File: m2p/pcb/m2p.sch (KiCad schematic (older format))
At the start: 78 parts, among them IC1 APU1205-HF-3, IC2 ADuM1201, IC3 SP100-2T, IC4 ADXL375, IC5 STM32F103C, P1 CONN_2, P2 CONN_4, P3 CONN_2, P4 SWD, P5 CONN_2, P6 CONN_2, Q1 MOSFET_P, Q2 MOSFET_P, Q3 MOSFET_N, Q4 MOSFET_N, U1 BAT BOX, U2 ARM SW, U3 RG LED, X1 8M

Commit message: add first go at m2r schematic
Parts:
- IC1: Farnell (none) -> 2319654
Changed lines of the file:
@@
 F 2 "" H 1650 850 60  0001 C CNN
 F 3 "" H 1650 850 60  0001 C CNN
+F 4 "2319654" H 1650 850 60  0001 C CNN "Farnell"
 	1    1650 850
 	1    0    0    -1

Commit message: finish up m2r schematic
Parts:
- added TP1, TP10, TP11, TP12, TP13, TP14, TP15, TP16, TP17, TP18, TP19, TP2, TP20, TP21, TP22, TP3, TP4, TP5, TP6, TP7, TP8, TP9: TESTPAD, symbol TESTPAD
- P3: Farnell (none) -> 1462926
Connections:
- net +BATT: now also TP1.1 (TP)
- net ACCEL_CS: now also TP9.1 (TP)
- net ACCEL_INT1: now also TP7.1 (TP)
- net ACCEL_INT2: now also TP8.1 (TP)
- net ACCEL_MISO: now also TP11.1 (TP)
- net ACCEL_MOSI: now also TP12.1 (TP)
- net ACCEL_SCK: now also TP10.1 (TP)
- net BARO_CS: now also TP19.1 (TP)
- net BARO_MISO: now also TP21.1 (TP)
- net BARO_MOSI: now also TP22.1 (TP)
- net BARO_SCK: now also TP20.1 (TP)
- net BAT_MON: now also TP6.1 (TP)
- net GND: now also TP3.1 (TP)
- net PYRO_1_C: now also TP16.1 (TP)
- net PYRO_1_F: now also TP15.1 (TP)
- net PYRO_2_C: now also TP18.1 (TP)
- net PYRO_2_F: now also TP17.1 (TP)
- net SER_IN: now also TP14.1 (TP)
- net SER_OUT: now also TP13.1 (TP)
- net VCC: now also TP2.1 (TP)
- net at IC2.7 (IN_A), P2.2 (P2): now also TP4.1 (TP)
- net at IC2.6 (OUT_B), P2.3 (P3): now also TP5.1 (TP)

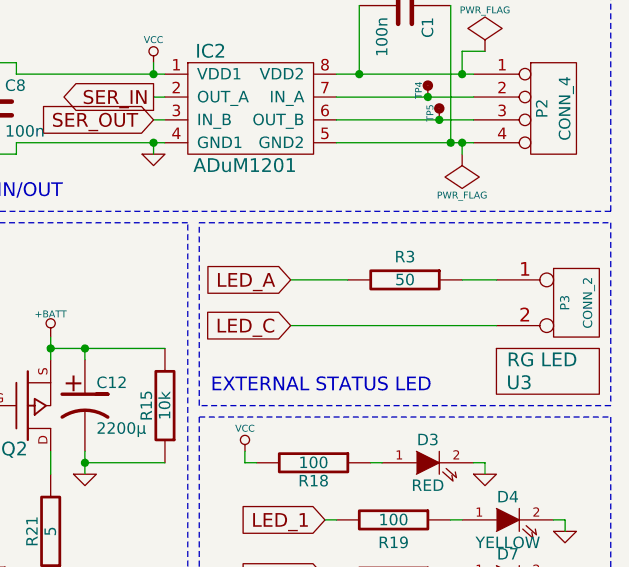
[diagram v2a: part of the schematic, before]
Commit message: swap 50R to two 100R on m2p too
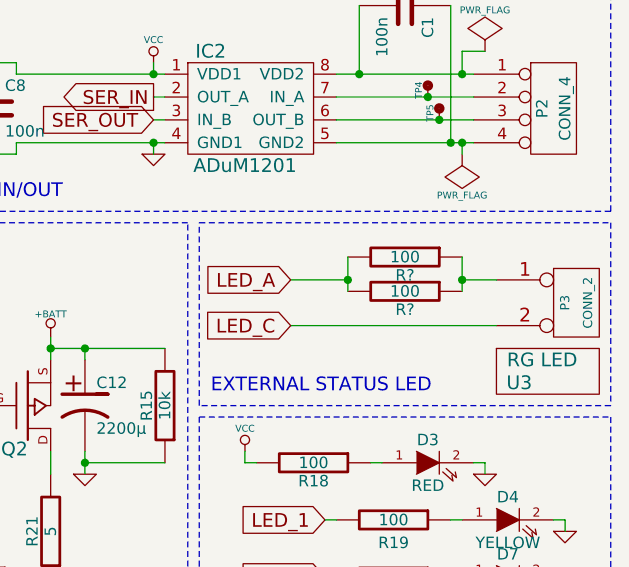
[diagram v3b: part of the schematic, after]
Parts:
- removed R3: 50, 0603, symbol R
- added R? (x2): 100, 0603, symbol R
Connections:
- net LED_A: now also R?.2, R?.2
- net at P3.1 (P1): now also R?.1, R?.1
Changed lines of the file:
@@
-	0    1    1    0
-$EndComp
-$Comp
-L R R3
-U 1 1 53683E31
-P 10250 1850
-F 0 "R3" V 10150 1850 50  0000 C CNN
-F 1 "50" V 10250 1850 50  0000 C CNN
-F 2 "0603" H 10250 1850 60  0001 C CNN
-F 3 "" H 10250 1850 60  0001 C CNN
-F 4 "2331983" V 10250 1850 60  0001 C CNN "Farnell"
-	1    10250 1850
 	0    1    1    0
 $EndComp
@@
 Connection ~ 10350 1050
 Connection ~ 10400 1150
+$Comp
+L R R?
+U 1 1 537E9CA5
+P 10250 1900
+F 0 "R?" V 10330 1900 50  0000 C CNN
+F 1 "100" V 10250 1900 50  0000 C CNN
+F 2 "0603" H 10250 1900 60  0001 C CNN
+F 3 "" H 10250 1900 60  0001 C CNN
+F 4 "2331989" V 10250 1900 60  0001 C CNN "Farnell"
+	1    10250 1900
+	0    1    1    0
+$EndComp
+$Comp
+L R R?
+U 1 1 537E9E87
+P 10250 1750
+F 0 "R?" V 10330 1750 50  0000 C CNN
+F 1 "100" V 10250 1750 50  0000 C CNN
+F 2 "0603" H 10250 1750 60  0001 C CNN
+F 3 "" H 10250 1750 60  0001 C CNN
+F 4 "2331989" V 10250 1750 60  0001 C CNN "Farnell"
+	1    10250 1750
+	0    1    1    0
+$EndComp
+Wire Wire Line
+	10000 1750 10000 1900
+Connection ~ 10000 1850
+Wire Wire Line
+	10500 1750 10500 1900
+Connection ~ 10500 1850
 $EndSCHEMATC

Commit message: oops, annotate
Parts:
- gave numbers to parts that had none: 2
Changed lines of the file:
@@
 Connection ~ 10400 1150
 $Comp
-L R R?
+L R R29
 U 1 1 537E9CA5
 P 10250 1900
-F 0 "R?" V 10330 1900 50  0000 C CNN
+F 0 "R29" V 10330 1900 50  0000 C CNN
 F 1 "100" V 10250 1900 50  0000 C CNN
 F 2 "0603" H 10250 1900 60  0001 C CNN
@@
 $EndComp
 $Comp
-L R R?
+L R R3
 U 1 1 537E9E87
 P 10250 1750
-F 0 "R?" V 10330 1750 50  0000 C CNN
+F 0 "R3" V 10330 1750 50  0000 C CNN
 F 1 "100" V 10250 1750 50  0000 C CNN
 F 2 "0603" H 10250 1750 60  0001 C CNN

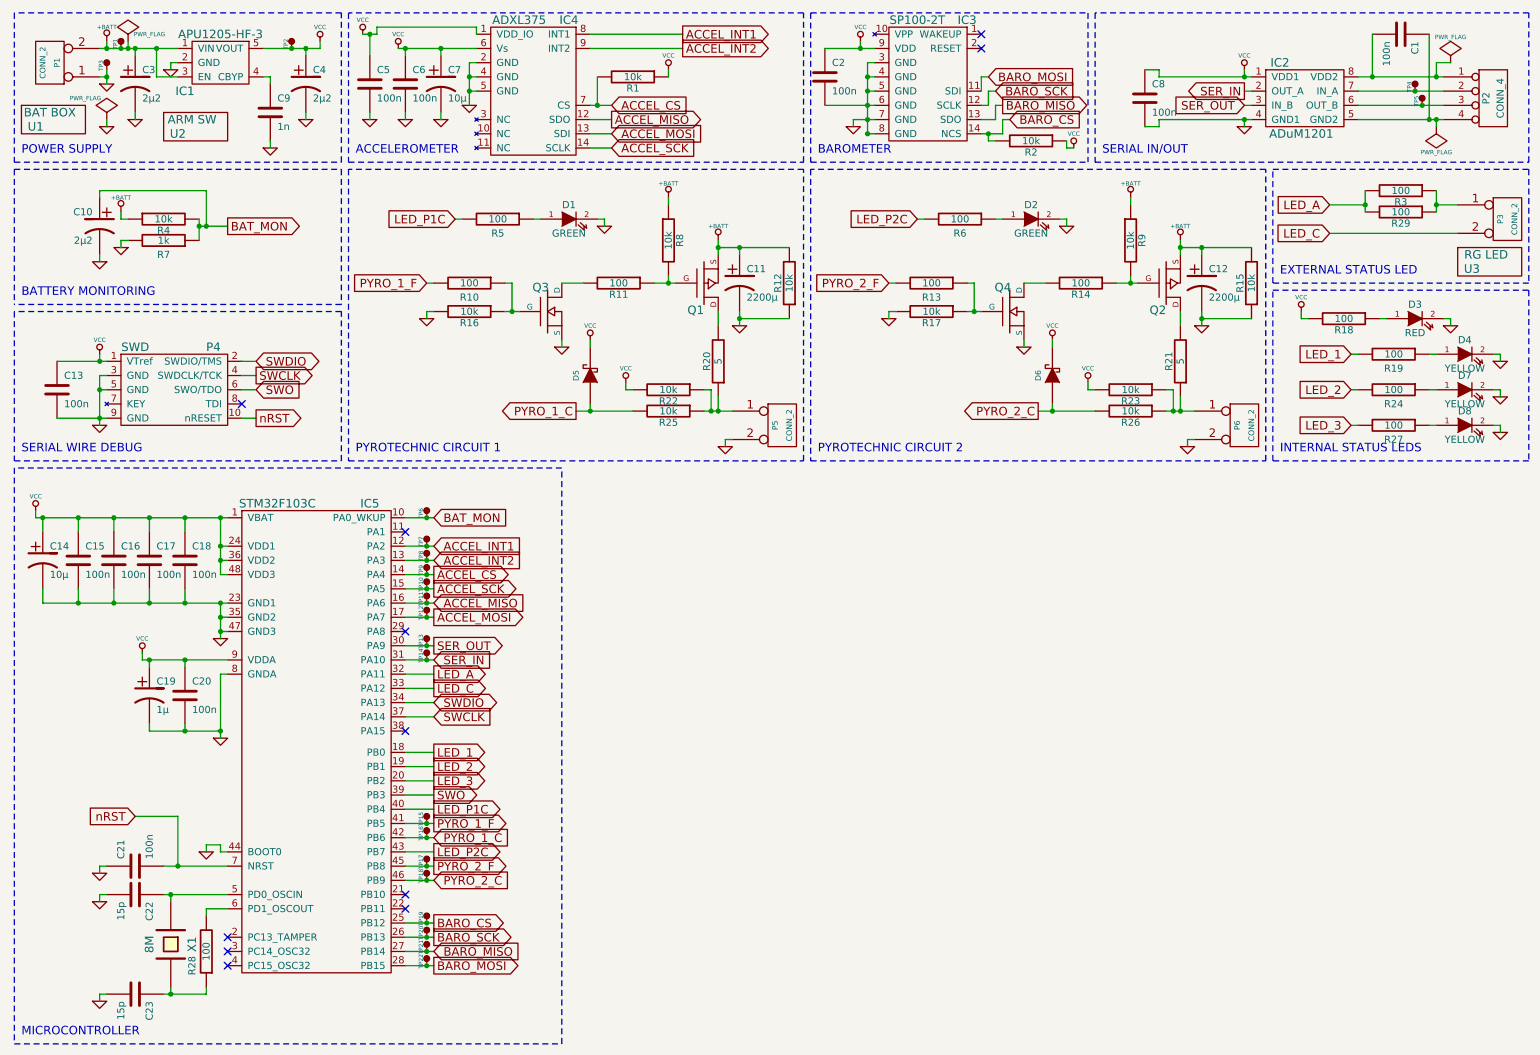
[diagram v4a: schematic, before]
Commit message: add separate connector for arming switch to m2p
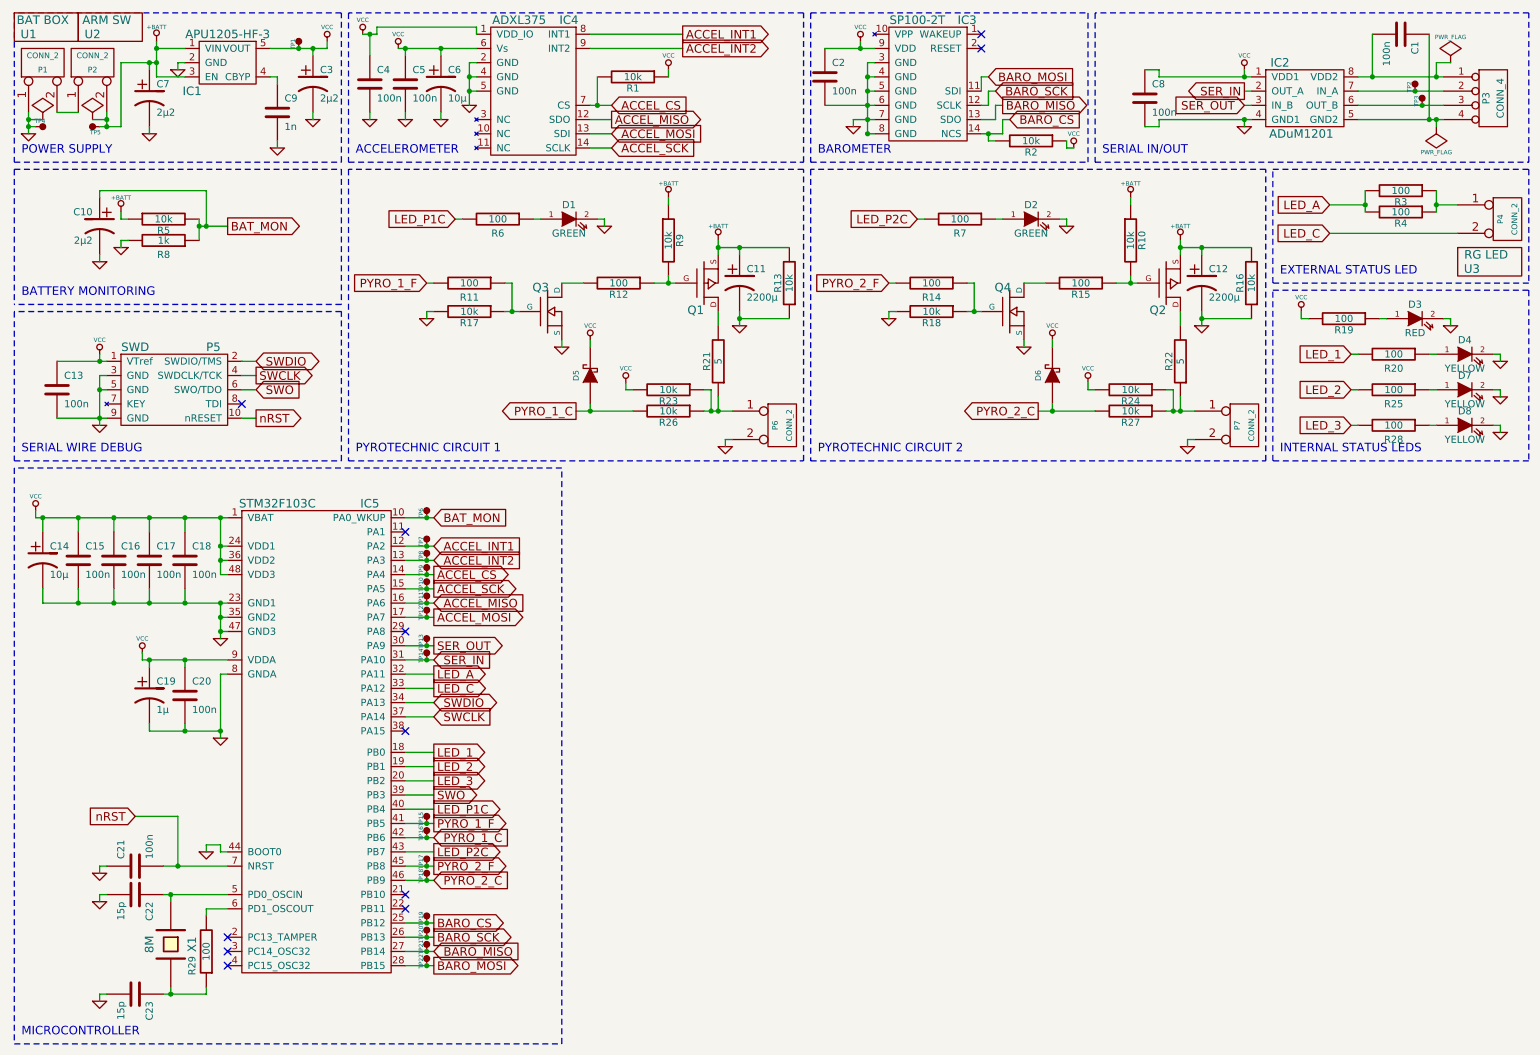
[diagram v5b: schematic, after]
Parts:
- added P2: CONN_2, symbol CONN_2
- renumbered C4 to C3, C5 to C4, C6 to C5, C7 to C6, C3 to C7, P2 to P3, P3 to P4, P4 to P5, P5 to P6, P6 to P7, R9 to R10, R10 to R11, R11 to R12, R12 to R13, R13 to R14, R14 to R15, R15 to R16, R16 to R17, R17 to R18, R18 to R19, R19 to R20, R20 to R21, R21 to R22, R22 to R23, R23 to R24, R24 to R25, R25 to R26, R26 to R27, R27 to R28, R28 to R29, R29 to R4, R4 to R5, R5 to R6, R6 to R7, R7 to R8, R8 to R9, TP2 to TP1, TP4 to TP2, TP5 to TP3, TP3 to TP4, TP1 to TP5
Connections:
- net +BATT: now also P2.2 (PM); no longer P1.2 (PM)
- new net: P1.2 (PM), P2.1 (P1)
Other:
- moved on the sheet: C3, C7, C9, IC1, P1, TP1, TP4, TP5, U1, U2

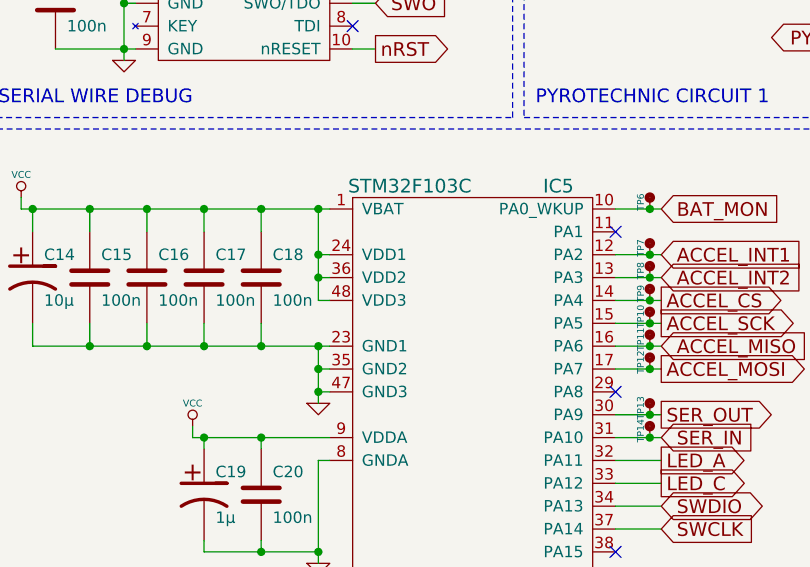
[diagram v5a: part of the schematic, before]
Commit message: Change F103 to F303 on m2p
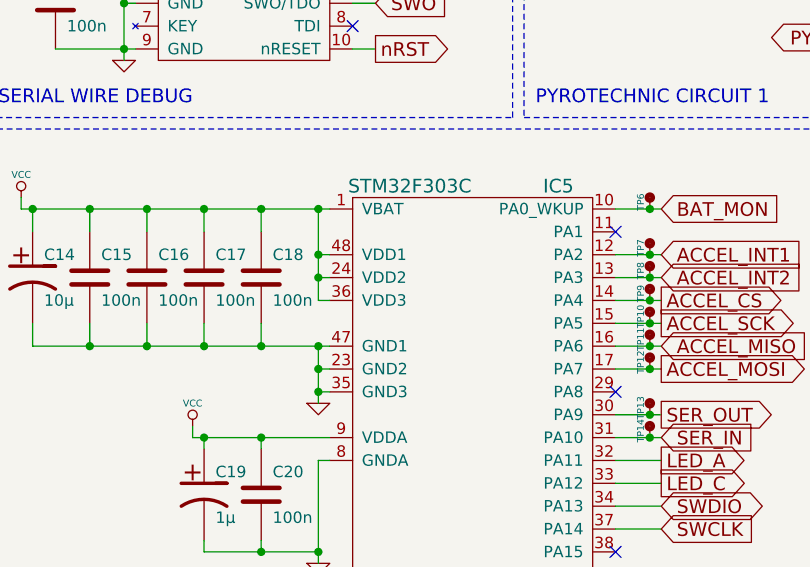
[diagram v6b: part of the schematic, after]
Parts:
- removed IC5: STM32F103C, LQFP48, symbol STM32F103C
- added IC5: STM32F303C, symbol STM32F303C
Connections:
- net ACCEL_CS: now also IC5.14 (PA4)
- net ACCEL_INT1: now also IC5.12 (PA2)
- net ACCEL_INT2: now also IC5.13 (PA3)
- net ACCEL_MISO: now also IC5.16 (PA6)
- net ACCEL_MOSI: now also IC5.17 (PA7)
- net ACCEL_SCK: now also IC5.15 (PA5)
- net BARO_CS: now also IC5.25 (PB12)
- net BARO_MISO: now also IC5.27 (PB14)
- net BARO_MOSI: now also IC5.28 (PB15)
- net BARO_SCK: now also IC5.26 (PB13)
- net BAT_MON: now also IC5.10 (PA0_WKUP)
- net GND: now also IC5.23 (GND2), IC5.35 (GND3), IC5.44 (BOOT0), IC5.47 (GND1), IC5.8 (GNDA)
- net LED_1: now also IC5.18 (PB0)
- net LED_2: now also IC5.19 (PB1)
- net LED_3: now also IC5.20 (PB2)
- net LED_A: now also IC5.32 (PA11)
- net LED_C: now also IC5.33 (PA12)
- net LED_P1C: now also IC5.40 (PB4)
- net LED_P2C: now also IC5.43 (PB7)
- net PYRO_1_C: now also IC5.42 (PB6)
- net PYRO_1_F: now also IC5.41 (PB5)
- net PYRO_2_C: now also IC5.46 (PB9)
- net PYRO_2_F: now also IC5.45 (PB8)
- net SER_IN: now also IC5.31 (PA10)
- net SER_OUT: now also IC5.30 (PA9)
- net SWCLK: now also IC5.37 (PA14)
- net SWDIO: now also IC5.34 (PA13)
- net SWO: now also IC5.39 (PB3)
- net VCC: now also IC5.1 (VBAT), IC5.24 (VDD2), IC5.36 (VDD3), IC5.48 (VDD1), IC5.9 (VDDA)
- net nRST: now also IC5.7 (NRST)
- net at C22.1, X1.1: now also IC5.5 (PD0_OSCIN)
- net at R29.2: now also IC5.6 (PD1_OSCOUT)
